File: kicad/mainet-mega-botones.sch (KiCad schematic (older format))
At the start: 4 parts, among them SW1 SW_Push_LED, SW2 SW_Push_LED, SW3 SW_Push_LED, SW4 SW_Push_LED

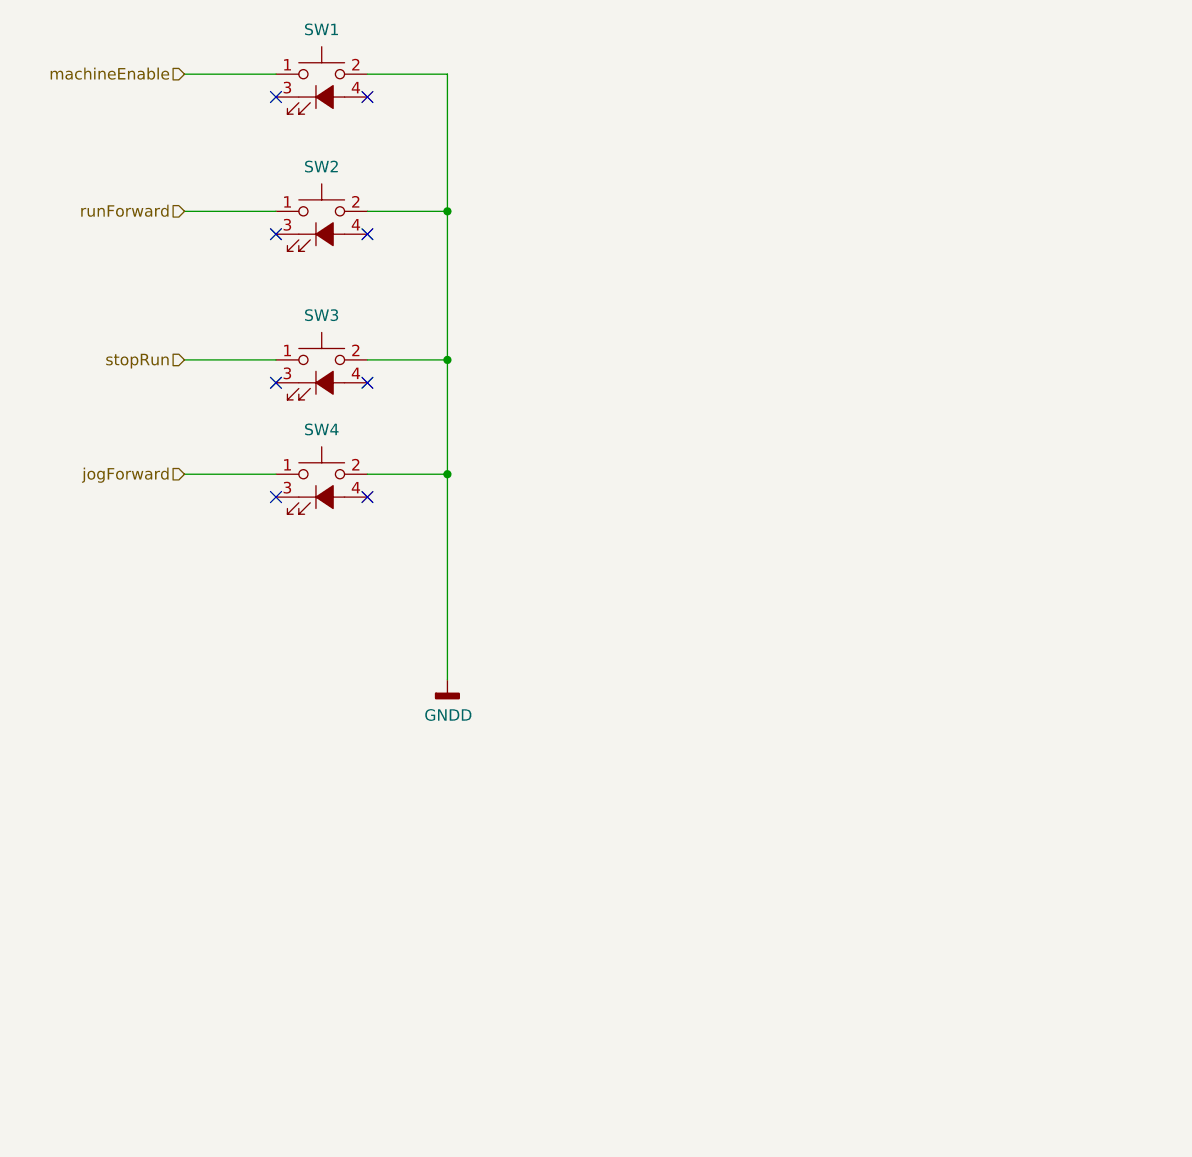
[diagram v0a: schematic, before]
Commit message: Kicad: Modificaciones menores esquemáticos
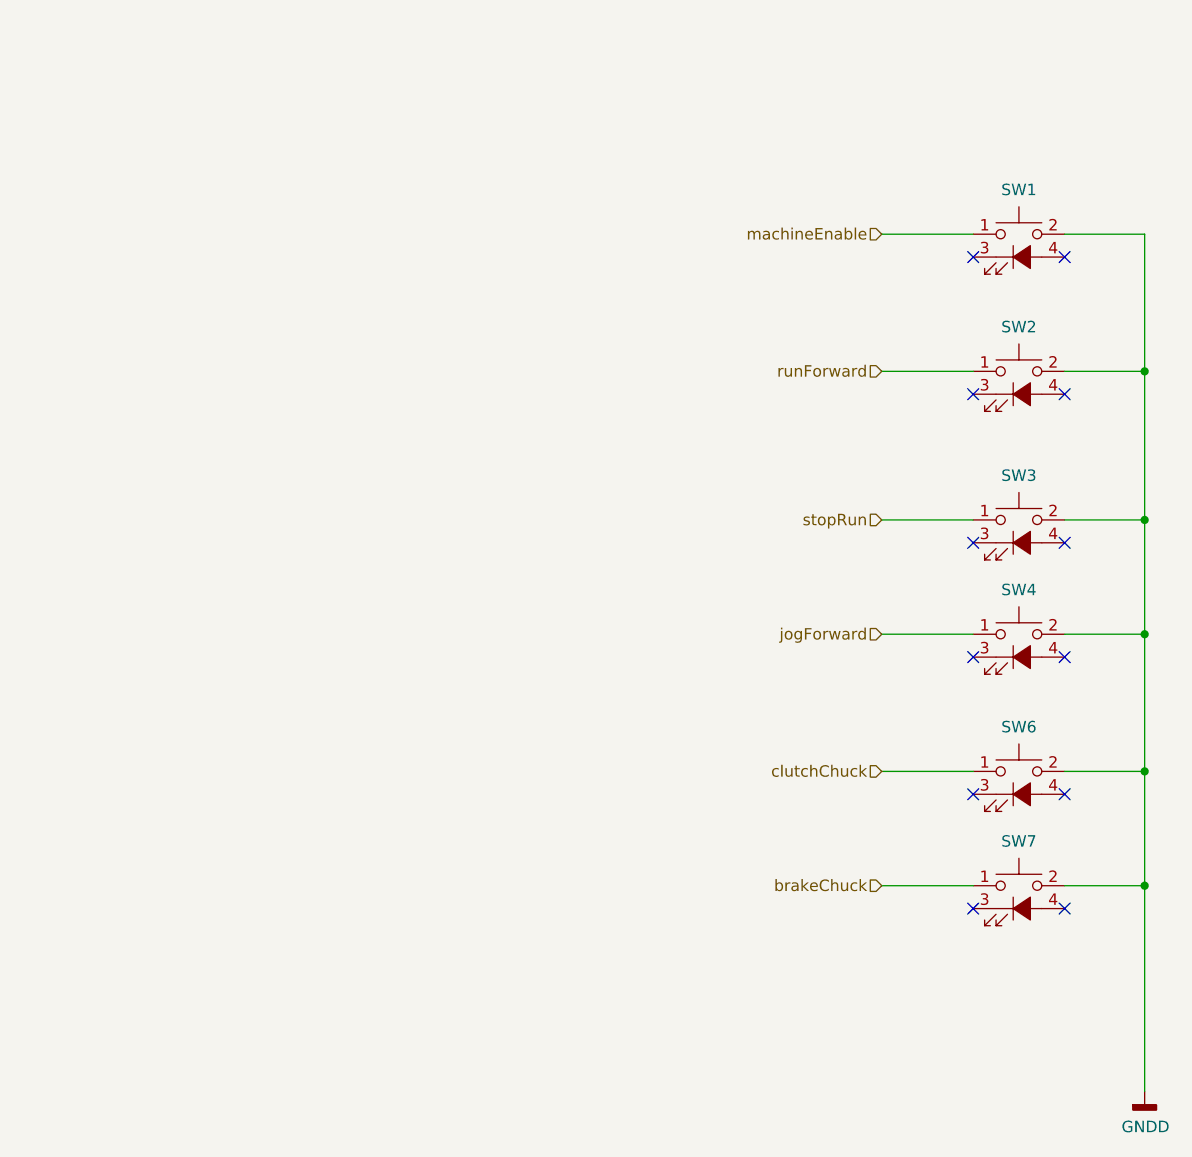
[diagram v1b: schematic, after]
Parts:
- added SW6, SW7: SW_Push_LED, symbol Switch:SW_Push_LED
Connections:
- net GNDD: now also SW6.2, SW7.2
- new net brakeChuck: SW7.1
- new net clutchChuck: SW6.1
- no-connect marks 8 -> 12
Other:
- moved on the sheet: SW1, SW2, SW3, SW4
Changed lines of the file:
@@
 $Descr A4 11693 8268
 encoding utf-8
-Sheet 4 17
+Sheet 6 17
 Title ""
 Date ""
@@
 Comment4 ""
 $EndDescr
-Text HLabel 1950 2000 0    50   Input ~ 0
+Text HLabel 5000 2700 0    50   Input ~ 0
 runForward
-Text HLabel 1950 2650 0    50   Input ~ 0
+Text HLabel 5000 3350 0    50   Input ~ 0
 stopRun
-Text HLabel 1950 3150 0    50   Input ~ 0
+Text HLabel 5000 3850 0    50   Input ~ 0
 jogForward
-Text HLabel 1950 1400 0    50   Input ~ 0
+Text HLabel 5000 2100 0    50   Input ~ 0
 machineEnable
 $Comp
 L Switch:SW_Push_LED SW1
 U 1 1 5FD984AF
-P 2550 1500
-F 0 "SW1" H 2550 1794 50  0000 C CNN
-F 1 "SW_Push_LED" V 2505 1398 50  0001 R CNN
-F 2 "" H 2550 1800 50  0001 C CNN
-F 3 "~" H 2550 1800 50  0001 C CNN
-	1    2550 1500
+P 5600 2200
+F 0 "SW1" H 5600 2494 50  0000 C CNN
+F 1 "SW_Push_LED" V 5555 2098 50  0001 R CNN
+F 2 "" H 5600 2500 50  0001 C CNN
+F 3 "~" H 5600 2500 50  0001 C CNN
+	1    5600 2200
 	1    0    0    -1
 $EndComp
@@
 L Switch:SW_Push_LED SW2
 U 1 1 5FD98B79
-P 2550 2100
-F 0 "SW2" H 2550 2394 50  0000 C CNN
-F 1 "SW_Push_LED" V 2505 1998 50  0001 R CNN
-F 2 "" H 2550 2400 50  0001 C CNN
-F 3 "~" H 2550 2400 50  0001 C CNN
-	1    2550 2100
+P 5600 2800
+F 0 "SW2" H 5600 3094 50  0000 C CNN
+F 1 "SW_Push_LED" V 5555 2698 50  0001 R CNN
+F 2 "" H 5600 3100 50  0001 C CNN
+F 3 "~" H 5600 3100 50  0001 C CNN
+	1    5600 2800
 	1    0    0    -1
 $EndComp
@@
 L Switch:SW_Push_LED SW3
 U 1 1 5FD98D8D
-P 2550 2750
-F 0 "SW3" H 2550 3044 50  0000 C CNN
-F 1 "SW_Push_LED" V 2505 2648 50  0001 R CNN
-F 2 "" H 2550 3050 50  0001 C CNN
-F 3 "~" H 2550 3050 50  0001 C CNN
-	1    2550 2750
+P 5600 3450
+F 0 "SW3" H 5600 3744 50  0000 C CNN
+F 1 "SW_Push_LED" V 5555 3348 50  0001 R CNN
+F 2 "" H 5600 3750 50  0001 C CNN
+F 3 "~" H 5600 3750 50  0001 C CNN
+	1    5600 3450
 	1    0    0    -1
 $EndComp
@@
 L Switch:SW_Push_LED SW4
 U 1 1 5FD9920E
-P 2550 3250
-F 0 "SW4" H 2550 3544 50  0000 C CNN
-F 1 "SW_Push_LED" V 2505 3148 50  0001 R CNN
-F 2 "" H 2550 3550 50  0001 C CNN
-F 3 "~" H 2550 3550 50  0001 C CNN
-	1    2550 3250
+P 5600 3950
+F 0 "SW4" H 5600 4244 50  0000 C CNN
+F 1 "SW_Push_LED" V 5555 3848 50  0001 R CNN
+F 2 "" H 5600 4250 50  0001 C CNN
+F 3 "~" H 5600 4250 50  0001 C CNN
+	1    5600 3950
 	1    0    0    -1
 $EndComp
@@
 L power:GNDD #PWR011
 U 1 1 5FD9A0E0
-P 3100 4050
-F 0 "#PWR011" H 3100 3800 50  0001 C CNN
-F 1 "GNDD" H 3104 3895 50  0000 C CNN
-F 2 "" H 3100 4050 50  0001 C CNN
-F 3 "" H 3100 4050 50  0001 C CNN
-	1    3100 4050
+P 6150 5850
+F 0 "#PWR011" H 6150 5600 50  0001 C CNN
+F 1 "GNDD" H 6154 5695 50  0000 C CNN
+F 2 "" H 6150 5850 50  0001 C CNN
+F 3 "" H 6150 5850 50  0001 C CNN
+	1    6150 5850
 	1    0    0    -1
 $EndComp
 Wire Wire Line
-	1950 1400 2350 1400
+	5000 2100 5400 2100
 Wire Wire Line
-	1950 2000 2350 2000
+	5000 2700 5400 2700
 Wire Wire Line
-	1950 2650 2350 2650
+	5000 3350 5400 3350
 Wire Wire Line
-	1950 3150 2350 3150
+	5000 3850 5400 3850
 Wire Wire Line
-	2750 1400 3100 1400
+	5800 2100 6150 2100
 Wire Wire Line
-	3100 1400 3100 2000
+	6150 2100 6150 2700
 Wire Wire Line
-	2750 2000 3100 2000
-Connection ~ 3100 2000
+	5800 2700 6150 2700
+Connection ~ 6150 2700
 Wire Wire Line
-	3100 2000 3100 2650
+	6150 2700 6150 3350
 Wire Wire Line
-	2750 2650 3100 2650
-Connection ~ 3100 2650
+	5800 3350 6150 3350
+Connection ~ 6150 3350
 Wire Wire Line
-	3100 2650 3100 3150
+	6150 3350 6150 3850
 Wire Wire Line
-	2750 3150 3100 3150
-Connection ~ 3100 3150
+	5800 3850 6150 3850
+NoConn ~ 5400 2200
+NoConn ~ 5400 2800
+NoConn ~ 5400 3450
+NoConn ~ 5400 3950
+NoConn ~ 5800 2800
+NoConn ~ 5800 2200
+NoConn ~ 5800 3450
+NoConn ~ 5800 3950
+Text HLabel 5000 4450 0    50   Input ~ 0
+clutchChuck
+Text HLabel 5000 4950 0    50   Input ~ 0
+brakeChuck
+$Comp
+L Switch:SW_Push_LED SW6
+U 1 1 601DBF1A
+P 5600 4550
+F 0 "SW6" H 5600 4844 50  0000 C CNN
+F 1 "SW_Push_LED" V 5555 4448 50  0001 R CNN
+F 2 "" H 5600 4850 50  0001 C CNN
+F 3 "~" H 5600 4850 50  0001 C CNN
+	1    5600 4550
+	1    0    0    -1
+$EndComp
+$Comp
+L Switch:SW_Push_LED SW7
+U 1 1 601DBF20
+P 5600 5050
+F 0 "SW7" H 5600 5344 50  0000 C CNN
+F 1 "SW_Push_LED" V 5555 4948 50  0001 R CNN
+F 2 "" H 5600 5350 50  0001 C CNN
+F 3 "~" H 5600 5350 50  0001 C CNN
+	1    5600 5050
+	1    0    0    -1
+$EndComp
 Wire Wire Line
-	3100 3150 3100 4050
-NoConn ~ 2350 1500
-NoConn ~ 2350 2100
-NoConn ~ 2350 2750
-NoConn ~ 2350 3250
-NoConn ~ 2750 2100
-NoConn ~ 2750 1500
-NoConn ~ 2750 2750
-NoConn ~ 2750 3250
+	5000 4450 5400 4450
+Wire Wire Line
+	5000 4950 5400 4950
+Wire Wire Line
+	5800 4450 6150 4450
+Wire Wire Line
+	6150 4450 6150 4950
+Wire Wire Line
+	5800 4950 6150 4950
+Connection ~ 6150 4950
+Wire Wire Line
+	6150 4950 6150 5850
+NoConn ~ 5400 4550
+NoConn ~ 5400 5050
+NoConn ~ 5800 4550
+NoConn ~ 5800 5050
+Wire Wire Line
+	6150 3850 6150 4450
+Connection ~ 6150 3850
+Connection ~ 6150 4450
 $EndSCHEMATC
